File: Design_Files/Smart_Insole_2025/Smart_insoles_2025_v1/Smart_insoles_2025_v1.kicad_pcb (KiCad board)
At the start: 4 copper layers, 69.7 x 30.1 mm, 51 parts, among them J1 Conn_01x20, J3 S2B-PH-SM4-TB_LF__SN_, U1 ESP32-C3_SUPERMINI_SMD, U2 CD74HC4067M96, U3 LSM6DSO32TR, U8 MCP6004-I_ST, U9 MCP6004-I_ST

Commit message: PCB new moving things around
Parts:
- C1, C2, C3: value 1uF -> 0.1uF
- moved C16 53.5 mm to (96.6, 27.1)
- moved R1 50.0 mm to (96.1, 30.6)
- moved C1 48.4 mm to (99.5, 44.7), turned to 0 degrees
- moved D2 29.0 mm to (127.3, 46.4), turned to 90 degrees
- moved D1 26.5 mm to (130.3, 44.4)
- moved R21 24.8 mm to (125.4, 46.4), turned to 90 degrees
- moved R20 17.0 mm to (133.5, 44.4), turned to 180 degrees
- moved C19 16.5 mm to (138.2, 46.4)
- moved R13 15.7 mm to (138.2, 47.9), turned to 180 degrees
- moved C18 1.34 mm to (112.7, 47.1), turned to 180 degrees
- moved R8 1.29 mm to (129.4, 36.5), turned to 0 degrees
- moved R18 0.98 mm to (112.7, 45.6), turned to 0 degrees
- moved R6 0.95 mm to (129.4, 34.9), turned to 0 degrees
- moved U8 0.87 mm to (135.0, 35.7)
- moved C3 0.78 mm to (125.0, 22.8)
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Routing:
- net /INT: track 0.00 -> 59.2 mm
- net GND: track 0.00 -> 46.6 mm, vias 0 -> 37
- net /I7: track 0.00 -> 29.1 mm
- net /I5: track 0.00 -> 27.0 mm
- net /I4: track 0.00 -> 24.5 mm
- net /I2: track 0.00 -> 23.8 mm
- net /I1: track 0.00 -> 23.7 mm
- net /I3: track 0.00 -> 22.7 mm
- net /I0: track 0.00 -> 19.9 mm
- net /I6: track 0.00 -> 18.0 mm
- net /FSR_AnalogFE/FSR_OUT_1: track 0.00 -> 14.4 mm
- net /FSR_AnalogFE/FSR_OUT_0: track 0.00 -> 10.4 mm
- net /FSR_AnalogFE/FSR_OUT_4: track 0.00 -> 10.2 mm
- net /FSR_AnalogFE/FSR_OUT_6: track 0.00 -> 7.32 mm
- net /FSR_AnalogFE/FSR_OUT_2: track 0.00 -> 7.07 mm
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
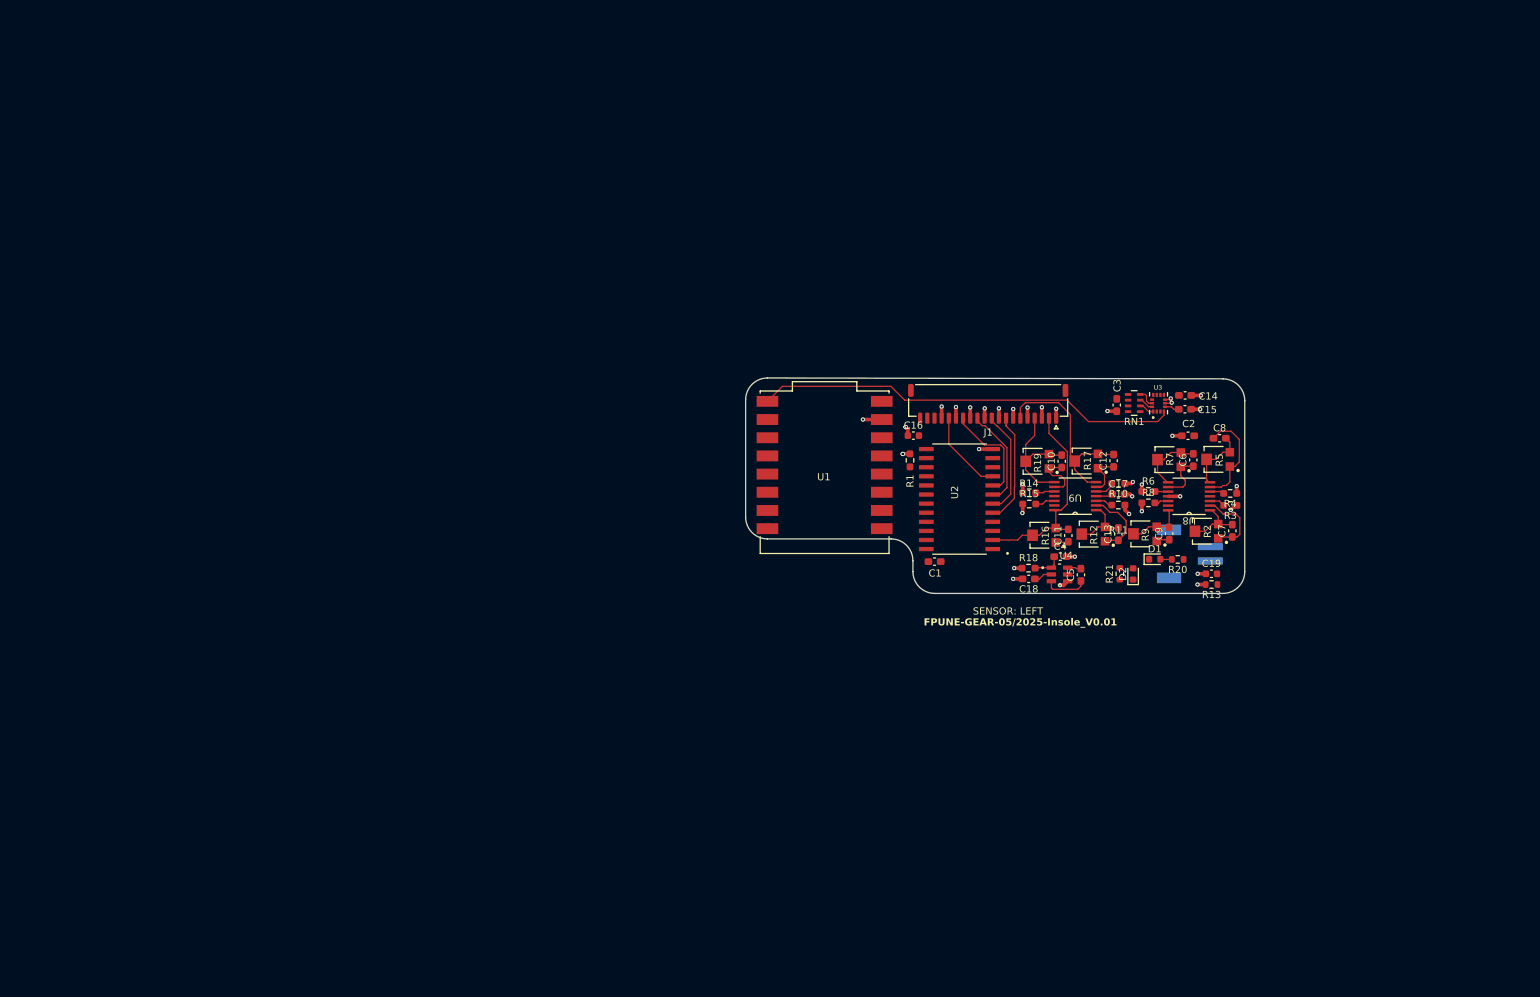
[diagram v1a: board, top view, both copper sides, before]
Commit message: SCH: Added missing footprints. PCB: Grouped related components for new layout
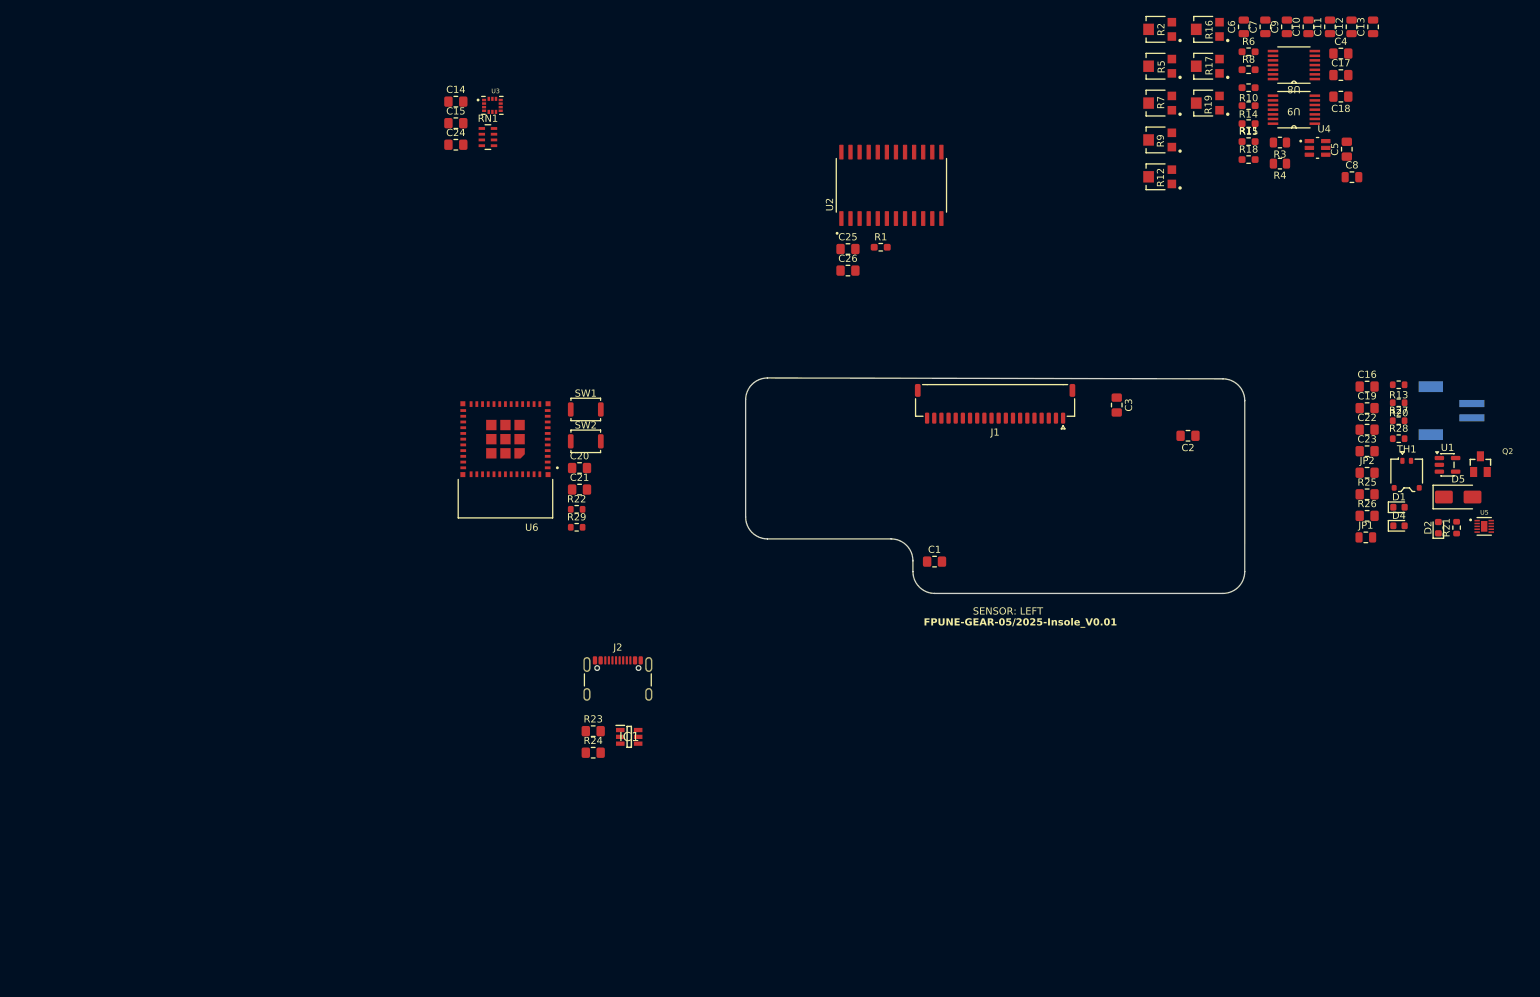
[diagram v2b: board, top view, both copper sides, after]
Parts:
- added C20: 0.1uF, Capacitor_SMD:C_0805_2012Metric_Pad1.18x1.45mm_HandSolder, F.Cu at (50.0, 31.6)
- added C21: 0.1uF, Capacitor_SMD:C_0805_2012Metric_Pad1.18x1.45mm_HandSolder, F.Cu at (50.0, 34.6)
- added C22: 1uF, Capacitor_SMD:C_0805_2012Metric_Pad1.18x1.45mm_HandSolder, F.Cu at (160.0, 26.3)
- added C23: 1uF, Capacitor_SMD:C_0805_2012Metric_Pad1.18x1.45mm_HandSolder, F.Cu at (160.0, 29.3)
- added C24: 100nF, Capacitor_SMD:C_0805_2012Metric_Pad1.18x1.45mm_HandSolder, F.Cu at (32.7, -13.5)
- added C25: 100nF, Capacitor_SMD:C_0805_2012Metric_Pad1.18x1.45mm_HandSolder, F.Cu at (87.4, 1.04)
- added C26: 1uF, Capacitor_SMD:C_0805_2012Metric_Pad1.18x1.45mm_HandSolder, F.Cu at (87.4, 4.05)
- added D4: LED, LED_SMD:LED_0603_1608Metric, F.Cu at (164.4, 39.7)
- added D5: SS24, Diode_SMD:D_SMA, F.Cu at (172.7, 35.7)
- added IC1: USBLC6-2SC6, USBLC6-2SC6:SOT95P280X145-6N, F.Cu at (56.9, 69.2)
- added J2: USB_C_Receptacle_USB2.0_16P, Connector_USB:USB_C_Receptacle_GCT_USB4105-xx-A_16P_TopMnt_Horizontal, F.Cu at (55.3, 62.2)
- added JP1: SolderJumper_2_Open, Capacitor_SMD:C_0805_2012Metric, F.Cu at (159.8, 41.3)
- added JP2: SolderJumper_2_Open, Capacitor_SMD:C_0805_2012Metric_Pad1.18x1.45mm_HandSolder, F.Cu at (160.0, 32.3)
- added Q2: FDN306P, FDN306P:SSOT-3, F.Cu at (175.8, 31.1)
- added R22: 10k, Resistor_SMD:R_0603_1608Metric, F.Cu at (49.5, 37.4)
- added R23: 5.1k 1%, Capacitor_SMD:C_0805_2012Metric_Pad1.18x1.45mm_HandSolder, F.Cu at (51.9, 68.4)
- added R24: 5.1k 1%, Capacitor_SMD:C_0805_2012Metric_Pad1.18x1.45mm_HandSolder, F.Cu at (51.9, 71.4)
- added R25: 1k, Capacitor_SMD:C_0805_2012Metric_Pad1.18x1.45mm_HandSolder, F.Cu at (160.0, 35.3)
- added R26: 10k, Capacitor_SMD:C_0805_2012Metric_Pad1.18x1.45mm_HandSolder, F.Cu at (160.0, 38.3)
- added R27: 2.0k, Resistor_SMD:R_0603_1608Metric, F.Cu at (164.4, 25.0)
- added R28: 1.5k, Resistor_SMD:R_0603_1608Metric, F.Cu at (164.4, 27.5)
- added R29: 10k, Resistor_SMD:R_0603_1608Metric, F.Cu at (49.5, 39.9)
- added SW1: RESET, Button_Switch_SMD:SW_Push_SPST_NO_Alps_SKRK, F.Cu at (50.8, 23.4)
- added SW2: BOOT, Button_Switch_SMD:SW_Push_SPST_NO_Alps_SKRK, F.Cu at (50.8, 27.9)
- added TH1: Thermistor_NTC, Connector_JST:JST_ACH_BM02B-ACHSS-GAN-ETF_1x02-1MP_P1.20mm_Vertical, F.Cu at (165.5, 32.5)
- added U5: BQ24040DSQR, BQ24040DSQR:SON40P200X200X80-11N, F.Cu at (176.3, 39.8)
- added U6: ESP32-C3-MINI-1-N4, ESP32-C3-MINI-1-N4:XCVR_ESP32-C3-MINI-1-N4, F.Cu at (39.6, 30.3)
- C1, C15, C17, C18, C2, C4, C5: footprint Capacitor_SMD:C_0603_1608Metric_Pad1.08x0.95mm_HandSolder -> Capacitor_SMD:C_0805_2012Metric_Pad1.18x1.45mm_HandSolder
- C10, C11, C12, C13, C6, C7, C8, C9: footprint Capacitor_SMD:C_0603_1608Metric_Pad1.08x0.95mm_HandSolder -> Capacitor_SMD:C_0805_2012Metric
- C14: value 100nF -> 1uF; footprint Capacitor_SMD:C_0603_1608Metric_Pad1.08x0.95mm_HandSolder -> Capacitor_SMD:C_0805_2012Metric_Pad1.18x1.45mm_HandSolder
- C16, C19: footprint Capacitor_SMD:C_0603_1608Metric -> Capacitor_SMD:C_0805_2012Metric_Pad1.18x1.45mm_HandSolder
- C3: value 0.1uF -> 1uF; footprint Capacitor_SMD:C_0603_1608Metric_Pad1.08x0.95mm_HandSolder -> Capacitor_SMD:C_0805_2012Metric_Pad1.18x1.45mm_HandSolder
- R13: value 540 -> 1.1k
- R3, R4: footprint Resistor_SMD:R_0603_1608Metric_Pad0.98x0.95mm_HandSolder -> Resistor_SMD:R_0805_2012Metric
- U1: value ESP32-C3_SUPERMINI_SMD -> ME6211C33M5; footprint ESP32-C3_SUPERMINI:MODULE_ESP32-C3_SUPERMINI -> Package_TO_SOT_SMD:SOT-23-5
- moved C14 109.8 mm to (32.7, -19.6)
- moved C15 109.4 mm to (32.7, -16.5)
- moved U3 101.9 mm to (37.8, -19.0), turned to 0 degrees
- moved RN1 97.6 mm to (37.1, -14.6), turned to 0 degrees
- moved U1 87.0 mm to (171.2, 31.2)
- moved C4 80.5 mm to (156.3, -26.3)
- moved C18 80.2 mm to (156.3, -20.2)
- moved C11 79.9 mm to (154.8, -30.0)
- moved C13 79.3 mm to (160.8, -30.0)
- moved R16 74.3 mm to (137.6, -29.6)
- moved C9 72.7 mm to (148.8, -30.0)
- moved C7 70.6 mm to (145.8, -30.0)
- moved R2 70.4 mm to (130.9, -29.6)
- moved C5 70.1 mm to (157.1, -12.9)
- moved C10 69.8 mm to (151.8, -30.0)
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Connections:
- net +BATT renamed /Battery Circuit Options/VBat
- net /CS renamed CS
- net /SDO/SA0 renamed SDO/SA0
- net Net-(D1-A) renamed /Battery Circuit Options/OUT_~{PG}
- net Net-(D2-A) renamed /Battery Circuit Options/OUT_~{CHG}
- C1 pad 1: VCC -> +3V3
- C14 pad 1: VCC -> +3V3
- C15 pad 1: Net-(U3-VDDIO) -> +3V3
- C16 pad 2: /Battery Circuit Options/5V_IN -> Net-(D5-A)
- C17 pad 1: VCC -> +3V3
- C18 pad 1: VCC -> +3V3
- C2 pad 1: VCC -> +3V3
- C3 pad 1: VCC -> +3V3
- R13 pad 1: Net-(U5-ISET) -> /Battery Circuit Options/ISET
- RN1 pad 3: /SDA -> SDA
- RN1 pad 4: /SCL -> SCL
- RN1 pad 5: VCC -> +3V3
- RN1 pad 6: VCC -> +3V3
- RN1 pad 7: VCC -> +3V3
- RN1 pad 8: VCC -> +3V3
- U1 pad 1: /S1 -> /Battery Circuit Options/Vsel
- U1 pad 2: /S2 -> GND
- U1 pad 3: /S3 -> /Battery Circuit Options/Vsel
- U1 pad 4: /SIG -> unconnected-(U1-NC-Pad4)
- U1 pad 5: /INT -> +3V3
- U2 pad 1: /SIG -> SIG
- U2 pad 10: /S0 -> S0
- U2 pad 11: /S1 -> S1
- U2 pad 13: /S3 -> S3
- U2 pad 14: /S2 -> S2
- U2 pad 2: /I7 -> I7
- U2 pad 24: VCC -> +3V3
- U2 pad 3: /I6 -> I6
- U2 pad 4: /I5 -> I5
- U2 pad 5: /I4 -> I4
- U2 pad 6: /I3 -> I3
- U2 pad 7: /I2 -> I2
- U2 pad 8: /I1 -> I1
- U2 pad 9: /I0 -> I0
- U3 pad 13: /SCL -> SCL
- U3 pad 14: /SDA -> SDA
- U3 pad 4: /INT -> INT
- U3 pad 5: Net-(U3-VDDIO) -> +3V3
- U3 pad 8: VCC -> +3V3
- U4 pad 2: VCC -> +3V3
- U8 pad 4: VCC -> +3V3
- U9 pad 4: VCC -> +3V3
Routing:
- net /INT: track 59.2 -> 0.00 mm
- net GND: track 46.6 -> 0.00 mm, vias 37 -> 0
- net /I7: track 29.1 -> 0.00 mm
- net /I5: track 27.0 -> 0.00 mm
- net /I4: track 24.5 -> 0.00 mm
- net /I2: track 23.8 -> 0.00 mm
- net /I1: track 23.7 -> 0.00 mm
- net /I3: track 22.7 -> 0.00 mm
- net /I0: track 19.9 -> 0.00 mm
- net /I6: track 18.0 -> 0.00 mm
- net /FSR_AnalogFE/FSR_OUT_1: track 14.4 -> 0.00 mm
- net /FSR_AnalogFE/FSR_OUT_0: track 10.4 -> 0.00 mm
- net /FSR_AnalogFE/FSR_OUT_4: track 10.2 -> 0.00 mm
- net /FSR_AnalogFE/FSR_OUT_6: track 7.32 -> 0.00 mm
- net /FSR_AnalogFE/FSR_OUT_2: track 7.07 -> 0.00 mm
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
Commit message: SCH: Fixed Warnings. Added thermistor solder pads library.
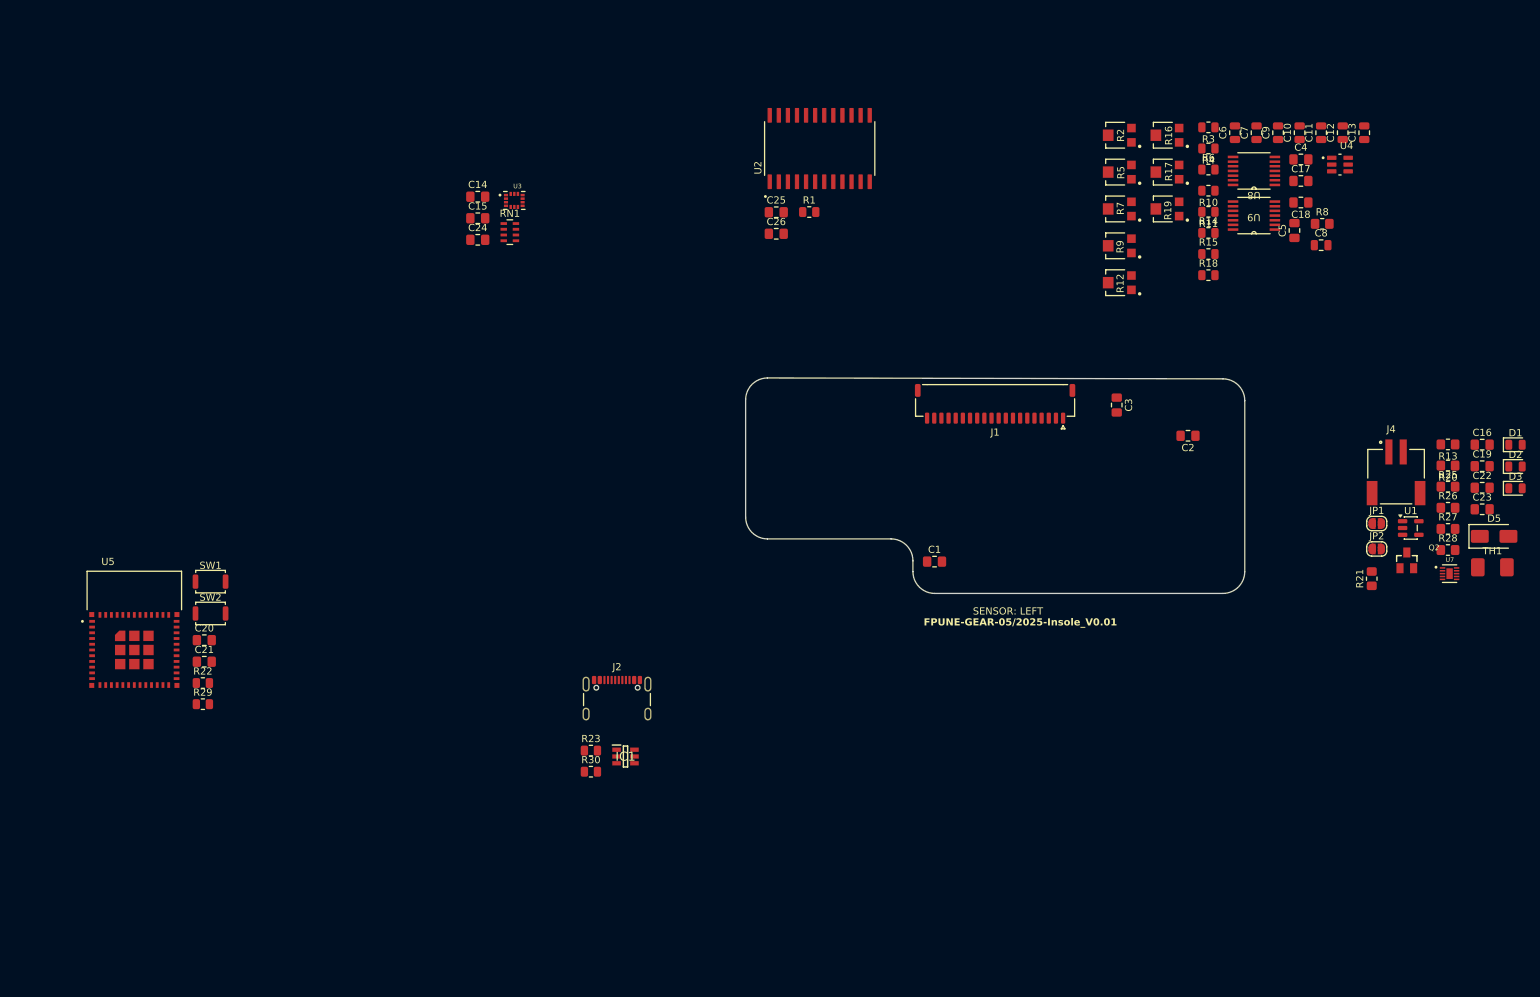
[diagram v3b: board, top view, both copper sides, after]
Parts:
- removed D4: LED, LED_SMD:LED_0603_1608Metric
- removed J3: S2B-PH-SM4-TB_LF__SN_, JST-PH2-2.00MM-SMD-HORIZONTAL:JST_S2B-PH-SM4-TB_LF__SN_
- removed R24: 5.1k 1%, Capacitor_SMD:C_0805_2012Metric_Pad1.18x1.45mm_HandSolder
- removed U6: ESP32-C3-MINI-1-N4, ESP32-C3-MINI-1-N4:XCVR_ESP32-C3-MINI-1-N4
- added D3: LED, LED_SMD:LED_0805_2012Metric, F.Cu at (180.7, 34.5)
- added J4: S2B-PH-SM4-TB_LF__SN_, JST-PH2-2.00MM-SMD-HORIZONTAL:JST_S2B-PH-SM4-TB_LF__SN_, F.Cu at (164.0, 29.4)
- added R30: 5.1k 1%, Resistor_SMD:R_0805_2012Metric, F.Cu at (51.5, 74.1)
- added U7: BQ24040DSQR, BQ24040DSQR:SON40P200X200X80-11N, F.Cu at (171.5, 46.4)
- D1, D2: footprint LED_SMD:LED_0603_1608Metric -> LED_SMD:LED_0805_2012Metric
- JP1: footprint Capacitor_SMD:C_0805_2012Metric -> Jumper:SolderJumper-2_P1.3mm_Open_RoundedPad1.0x1.5mm
- JP2: footprint Capacitor_SMD:C_0805_2012Metric_Pad1.18x1.45mm_HandSolder -> Jumper:SolderJumper-2_P1.3mm_Open_RoundedPad1.0x1.5mm
- R1, R10, R11, R14, R15, R18, R6: footprint Resistor_SMD:R_0603_1608Metric_Pad0.98x0.95mm_HandSolder -> Resistor_SMD:R_0805_2012Metric
- R13, R20, R21, R27, R28: footprint Resistor_SMD:R_0603_1608Metric -> Resistor_SMD:R_0805_2012Metric_Pad1.20x1.40mm_HandSolder
- R22, R29: footprint Resistor_SMD:R_0603_1608Metric -> Resistor_SMD:R_0805_2012Metric
- R23: footprint Capacitor_SMD:C_0805_2012Metric_Pad1.18x1.45mm_HandSolder -> Resistor_SMD:R_0805_2012Metric
- R25, R26: footprint Capacitor_SMD:C_0805_2012Metric_Pad1.18x1.45mm_HandSolder -> Resistor_SMD:R_0805_2012Metric_Pad1.20x1.40mm_HandSolder
- R8: footprint Resistor_SMD:R_0603_1608Metric_Pad0.98x0.95mm_HandSolder -> Resistor_SMD:R_0805_2012Metric_Pad1.20x1.40mm_HandSolder
- TH1: footprint Connector_JST:JST_ACH_BM02B-ACHSS-GAN-ETF_1x02-1MP_P1.20mm_Vertical -> thermistor_10k_NTC_solderPad:thermistor_10k_NTC_SolderPad
- U5: value BQ24040DSQR -> ESP32-C3-MINI-1-N4; footprint BQ24040DSQR:SON40P200X200X80-11N -> ESP32-C3-MINI-1-N4:XCVR_ESP32-C3-MINI-1-N4
- moved U5 189.1 mm to (-12.2, 54.4)
- moved R29 57.8 mm to (-2.67, 64.6)
- moved C20 57.7 mm to (-2.47, 55.7)
- moved C21 57.7 mm to (-2.47, 58.7)
- moved SW1 57.7 mm to (-1.60, 47.5)
- moved SW2 57.7 mm to (-1.60, 52.0)
- moved R22 57.6 mm to (-2.67, 61.7)
- moved R8 23.9 mm to (153.7, -2.48)
- moved D1 18.5 mm to (180.7, 28.4)
- moved C22 18.0 mm to (176.0, 34.4)
- moved C16 18.0 mm to (176.0, 28.4)
- moved C19 18.0 mm to (176.0, 31.4)
- moved C23 18.0 mm to (176.0, 37.4)
- moved TH1 17.7 mm to (177.5, 45.5)
- moved R6 17.4 mm to (137.8, -10.1)
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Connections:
- C10 pad 2: /I6 -> I6
- C11 pad 2: /I7 -> I7
- C12 pad 2: /I5 -> I5
- C13 pad 2: /I4 -> I4
- C20 pad 2: Net-(U6-IO9) -> Net-(U5-IO9)
- C21 pad 2: Net-(U6-EN) -> Net-(U5-EN)
- C6 pad 2: /I2 -> I2
- C7 pad 2: /I0 -> I0
- C8 pad 2: /I1 -> I1
- C9 pad 2: /I3 -> I3
- D1 pad 1: /Battery Circuit Options/~{PG} -> /Battery Circuit Options/~{CHG}
- D1 pad 2: /Battery Circuit Options/OUT_~{PG} -> /Battery Circuit Options/OUT_~{CHG}
- D2 pad 1: /Battery Circuit Options/~{CHG} -> GND
- D2 pad 2: /Battery Circuit Options/OUT_~{CHG} -> Net-(D2-A)
- J1 pad 10: /I3 -> /FSR_AnalogFE/FSR_OUT_4
- J1 pad 12: /I2 -> /FSR_AnalogFE/FSR_OUT_5
- J1 pad 14: /I1 -> /FSR_AnalogFE/FSR_OUT_6
- J1 pad 16: /I0 -> /FSR_AnalogFE/FSR_OUT_7
- J1 pad 2: /I7 -> /FSR_AnalogFE/FSR_OUT_0
- J1 pad 4: /I6 -> /FSR_AnalogFE/FSR_OUT_1
- J1 pad 6: /I5 -> /FSR_AnalogFE/FSR_OUT_2
- J1 pad 8: /I4 -> /FSR_AnalogFE/FSR_OUT_3
- R12 pad 2: /I4 -> I4
- R12 pad 3: /I4 -> I4
- R16 pad 2: /I7 -> I7
- R16 pad 3: /I7 -> I7
- R17 pad 2: /I5 -> I5
- R17 pad 3: /I5 -> I5
- R19 pad 2: /I6 -> I6
- R19 pad 3: /I6 -> I6
- R2 pad 2: /I0 -> I0
- R2 pad 3: /I0 -> I0
- R22 pad 2: Net-(U6-EN) -> Net-(U5-EN)
- R28 pad 2: Net-(D4-A) -> Net-(D2-A)
- R29 pad 2: Net-(U6-IO9) -> Net-(U5-IO9)
- R5 pad 2: /I1 -> I1
- R5 pad 3: /I1 -> I1
- R7 pad 2: /I2 -> I2
- R7 pad 3: /I2 -> I2
- R9 pad 2: /I3 -> I3
- R9 pad 3: /I3 -> I3
- SW1 pad 2: Net-(U6-EN) -> Net-(U5-EN)
- SW2 pad 2: Net-(U6-IO9) -> Net-(U5-IO9)
- U5 pad 1: Net-(D5-A) -> GND
- U5 pad 10: /Battery Circuit Options/VBat -> unconnected-(U5-NC__3-Pad10)
- U5 pad 2: /Battery Circuit Options/ISET -> GND
- U5 pad 3: GND -> +3V3
- U5 pad 4: /Battery Circuit Options/PRETERM -> unconnected-(U5-NC-Pad4)
- U5 pad 5: /Battery Circuit Options/~{PG} -> S2
- U5 pad 6: (no net) -> S3
- U5 pad 7: GND -> unconnected-(U5-NC__1-Pad7)
- U5 pad 8: /Battery Circuit Options/~{CHG} -> Net-(U5-EN)
- U5 pad 9: /Battery Circuit Options/TS -> unconnected-(U5-NC__2-Pad9)
- U8 pad 1: /I0 -> I0
- U8 pad 14: /I3 -> I3
- U8 pad 7: /I1 -> I1
- U8 pad 8: /I2 -> I2
- U9 pad 1: /I4 -> I4
- U9 pad 14: /I7 -> I7
- U9 pad 7: /I5 -> I5
- U9 pad 8: /I6 -> I6
